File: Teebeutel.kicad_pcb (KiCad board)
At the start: 2 copper layers, 72 x 100 mm, 154 parts, among them J1 RJ45_Shielded, J2 Battery, J3 Micro_SD_Card, J4 Conn_01x30_Female, Q1 S8050, Q2 S8050, SW1 K1-1506SN-01, SW2 SW_SPST, U1 LIS2DE12, U10 SDB628, U11 TLV1117-33, U12 SGP30, U2 ESP32-WROOM-32, U3 SRV05-4, U4 TXB0104RUT, U5 MCP73831-2-OT, U6 PPSI262, U7 RM-V8xxC_TR1, U8 TLV70018_SOT23-5, U9 TXB0104RUT

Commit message: chore(OSHWA): Add ID (DE000117)
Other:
- board text added: "ID: DE000117"
- board text removed: "ID: *TBA*"

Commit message: feat(ibom): add ibom
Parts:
- C1, C10, C11, C12, C13, C14, C15, C16, C17, C19, C2, C20, C22, C24, C25, C27, C3, C32, C35, C38, C5, C6, C7, C9: value 100n -> 100nF
- C18, C21, C23, C26, C29, C31, C37, C4, C40, C8: value 10µ -> 10µF
- C28, C30: value 1µ -> 1µF
- C33, C34: value 4,7µ -> 4,7µF
- D11, D19: value D -> DO-214AC
- L1: value L_Core_Iron -> 4,7µH
- R1, R10, R12, R14, R15, R17, R19, R2, R22, R23, R26, R3, R4, R5, R7, R9: value 10k -> 10kΩ
- R11: value 10 -> 10Ω
- R13: value 2k2 -> 2.2kΩ
- R16, R18, R6, R8: value 470 -> 470Ω
- R20: value 300k -> 300kΩ
- R21: value 100k -> 100KΩ
- R24: value 56 -> 56Ω
- R25: value 82 -> 82Ω
- R27: value 560k -> 560kΩ
- R28: value 620k 1% -> 620kΩ 1%
- R29: value 30k 1% -> 30kΩ 1%

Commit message: feat: more routing work
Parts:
- added C41: 10µF, Capacitor_SMD:C_0603_1608Metric, F.Cu at (117.0, 141.8)
- added C42: 100nF, Capacitor_SMD:C_0603_1608Metric, F.Cu at (115.5, 141.8)
- added C43: 100nF, Capacitor_SMD:C_0603_1608Metric, F.Cu at (257.8, 30.0)
- added C44: 10µF, Capacitor_SMD:C_0603_1608Metric, F.Cu at (260.8, 22.2)
- added D20: 1N4148WT, Diode_SMD:D_SOD-523, F.Cu at (118.5, 141.8)
- added J5: Conn_01x10_Female, Connector_PinSocket_2.54mm:PinSocket_1x10_P2.54mm_Vertical_SMD_Pin1Left, F.Cu at (173.9, 100.0)
- added J6: Conn_01x10_Female, Connector_PinSocket_2.54mm:PinSocket_1x10_P2.54mm_Vertical_SMD_Pin1Right, F.Cu at (118.1, 100.0)
- added M1: Motor_DC, Teebeutel_Special_Parts:LNLON-S3070P, F.Cu at (122.1, 141.8)
- added Q3: BSN20, Package_TO_SOT_SMD:SOT-23, F.Cu at (115.6, 145.0)
- added R30: 10kΩ, Resistor_SMD:R_0603_1608Metric, F.Cu at (113.0, 145.2)
- added R31: 10kΩ, Resistor_SMD:R_0603_1608Metric, F.Cu at (251.9, 26.1)
- added R32: 10kΩ, Resistor_SMD:R_0603_1608Metric, F.Cu at (251.7, 29.2)
- added R33: 10kΩ, Resistor_SMD:R_0603_1608Metric, F.Cu at (155.8, 114.5)
- added R34: 10kΩ, Resistor_SMD:R_0603_1608Metric, F.Cu at (165.2, 114.5)
- added TP33: VIBRATION, TestPoint:TestPoint_Pad_D1.0mm, F.Cu at (113.0, 147.8)
- added TP34: EXP-INT-B, TestPoint:TestPoint_Pad_D1.0mm, F.Cu at (264.3, 35.9)
- added TP35: EXP-~RST, TestPoint:TestPoint_Pad_D1.0mm, F.Cu at (263.0, 38.3)
- added U13: PCA9539BS,118, Teebeutel_Special_Parts:QFN50P400X400X100-25N-D, F.Cu at (160.5, 117.0)
- J2: footprint Connector_PinHeader_2.54mm:PinHeader_1x02_P2.54mm_Vertical -> Connector_Molex:Molex_PicoBlade_53261-0271_1x02-1MP_P1.25mm_Horizontal
- moved TP18 174.5 mm to (275.5, 38.1), turned to 0 degrees
- moved TP15 173.0 mm to (277.5, 36.6)
- moved TP14 161.6 mm to (275.0, 32.1)
- moved TP16 160.1 mm to (279.8, 34.3)
- moved TP17 158.9 mm to (278.7, 28.7)
- moved TP4 131.1 mm to (273.4, 72.9)
- moved TP5 129.0 mm to (273.6, 76.2)
- moved R10 125.4 mm to (268.2, 72.5), turned to 0 degrees
- moved R9 124.9 mm to (268.1, 75.5), turned to 0 degrees
- moved TP3 114.2 mm to (245.5, 123.4), turned to 0 degrees
- moved R4 113.9 mm to (242.9, 115.2), turned to 0 degrees
- moved TP1 113.3 mm to (242.4, 122.9), turned to 0 degrees
- moved Q1 110.4 mm to (238.7, 115.1), turned to 0 degrees
- moved R5 109.0 mm to (243.1, 118.3), turned to 0 degrees
- moved Q2 105.8 mm to (239.3, 120.3), turned to 0 degrees
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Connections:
- D12 pad 1: Net-(D12-Pad1) -> WS2812
- D12 pad 3: (no net) -> Net-(D12-Pad3)
- D13 pad 1: Net-(D10-Pad3) -> Net-(D1-Pad3)
- D13 pad 3: Net-(D1-Pad1) -> Net-(D10-Pad1)
- D2 pad 1: WS2812 -> Net-(D2-Pad1)
- D2 pad 3: Net-(D2-Pad3) -> WS2812-OUT
- D3 pad 1: Net-(D1-Pad3) -> Net-(D3-Pad1)
- D3 pad 3: Net-(D3-Pad3) -> Net-(D1-Pad1)
- D4 pad 1: Net-(D2-Pad3) -> Net-(D4-Pad1)
- D4 pad 3: Net-(D4-Pad3) -> Net-(D2-Pad1)
- D5 pad 1: Net-(D3-Pad3) -> Net-(D5-Pad1)
- D5 pad 3: Net-(D5-Pad3) -> Net-(D3-Pad1)
- D6 pad 1: Net-(D4-Pad3) -> Net-(D6-Pad1)
- D6 pad 3: Net-(D6-Pad3) -> Net-(D4-Pad1)
- D7 pad 1: Net-(D5-Pad3) -> Net-(D7-Pad1)
- D7 pad 3: Net-(D7-Pad3) -> Net-(D5-Pad1)
- D8 pad 1: Net-(D6-Pad3) -> Net-(D10-Pad3)
- D8 pad 3: Net-(D10-Pad1) -> Net-(D6-Pad1)
- D9 pad 1: Net-(D7-Pad3) -> Net-(D12-Pad3)
- D9 pad 3: Net-(D12-Pad1) -> Net-(D7-Pad1)
- J2 pad 1: GND -> Net-(C26-Pad1)
- J2 pad 2: Net-(C26-Pad1) -> GND
- J4 pad 14: +3V3 -> GND
- J4 pad 18: OLED-SDA -> OLED-MOSI
- TB1 pad 1: TOUCH9 -> TOUCH0
- TB2 pad 1: TOUCH4 -> TOUCH3
- TP27 pad 1: OLED-SDA -> (no net)
- U2 pad 10: (no net) -> I2C-SCL
- U2 pad 11: (no net) -> I2C-SDA
- U2 pad 12: TOUCH9 -> IR-TX
- U2 pad 13: OLED-SDA -> OLED-SCK
- U2 pad 14: OLED-SCK -> (no net)
- U2 pad 16: OLED-DC -> OLED-MOSI
- U2 pad 17: BTN_PUSH -> (no net)
- U2 pad 18: SD-SCK -> (no net)
- U2 pad 19: SD-MISO -> (no net)
- U2 pad 20: TOUCH4 -> (no net)
- U2 pad 21: BTN_UP -> (no net)
- U2 pad 22: BTN_DOWN -> (no net)
- U2 pad 23: SD-MOSI -> TOUCH3
- U2 pad 26: SD-CS -> TOUCH0
- U2 pad 29: I2C-SDA -> SD-CS
- U2 pad 30: I2C-SCL -> SD-SCK
- U2 pad 31: WS2812 -> SD-MISO
- U2 pad 33: BTN_LEFT -> OLED-DC
- U2 pad 34: TxD -> RxD
- U2 pad 35: RxD -> TxD
- U2 pad 36: BTN_RIGHT -> EXP-~RST
- U2 pad 37: IR-TX -> SD-MOSI
- U2 pad 6: (no net) -> EXP-~INT
- U2 pad 7: (no net) -> SPO2-INT
- U2 pad 8: (no net) -> WS2812
- U2 pad 9: (no net) -> ESP-ADC5
- U6 pad 9: (no net) -> SPO2-INT
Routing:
- net +3V3: track 568.0 -> 173.2 mm, vias 26 -> 4
- net I2C-SCL: track 106.5 -> 4.33 mm, vias 8 -> 2
- net I2C-SDA: track 99.9 -> 1.61 mm, vias 8 -> 0
- net VIBRATION: track 0.00 -> 73.9 mm, vias 0 -> 2
- net IR-TX: track 143.0 -> 70.7 mm
- net Net-(C26-Pad1): track 73.2 -> 2.94 mm
- net DTR: track 61.1 -> 0.00 mm, vias 2 -> 0
- net RTS: track 59.5 -> 0.00 mm, vias 2 -> 0
- net RxD: track 82.1 -> 24.0 mm, vias 3 -> 1
- net Net-(J1-Pad5): track 56.8 -> 0.00 mm, vias 1 -> 0
- net +5V: track 56.3 -> 0.00 mm, vias 4 -> 0
- net Net-(J1-Pad4): track 55.9 -> 0.00 mm
- net OLED-SDA: track 48.9 -> 0.00 mm, vias 2 -> 0
- net Net-(D14-Pad2): track 48.0 -> 0.00 mm
- net OLED-MOSI: track 0.00 -> 46.7 mm, vias 0 -> 2
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- removed copper zone on F.Cu, net +5V
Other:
- board text added: "3.3V"
- board text added: "BATTERY"
- board text added: "GND"
- board text added: "IO0"
- board text added: "IO1"
- board text added: "IO2"
- board text added: "IO3"
- board text added: "IO4"
- board text added: "IO5"
- board text added: "IO6"
- board text added: "IO7"
- board text added: "IO8"
- board text added: "IO9"
- board text added: "I²C"
- board text added: "LED"
- board text added: "RX"
- board text added: "SCL"
- board text added: "SDA"
- board text added: "SERIAL"
- board text added: "TX"
- board text added: "Teebeutel v1.0"
- board text added: "VIN"
- board text added: "teebeutel.entropia.de"
- board text removed: "Teebeutel v0.1"
- board text removed: "teebeutel.jadyn.dev"

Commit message: small changes
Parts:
- added R35: 10kΩ, Resistor_SMD:R_0603_1608Metric, F.Cu at (195.0, 67.5)
- Q3: value BSN20 -> AO3400
- REF**: value OSHW-Logo2_7.3x6mm_SilkScreen -> OSHW-Logo2_9.8x8mm_SilkScreen; footprint Symbol:OSHW-Logo2_7.3x6mm_SilkScreen -> Symbol:OSHW-Logo2_9.8x8mm_SilkScreen
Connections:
- U6 pad 13: (no net) -> Net-(R35-Pad1)
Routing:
- net SD-MOSI: track 24.2 -> 25.3 mm
- net VIBRATION: track 73.9 -> 74.9 mm
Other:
- outline, holes or cut-outs redrawn

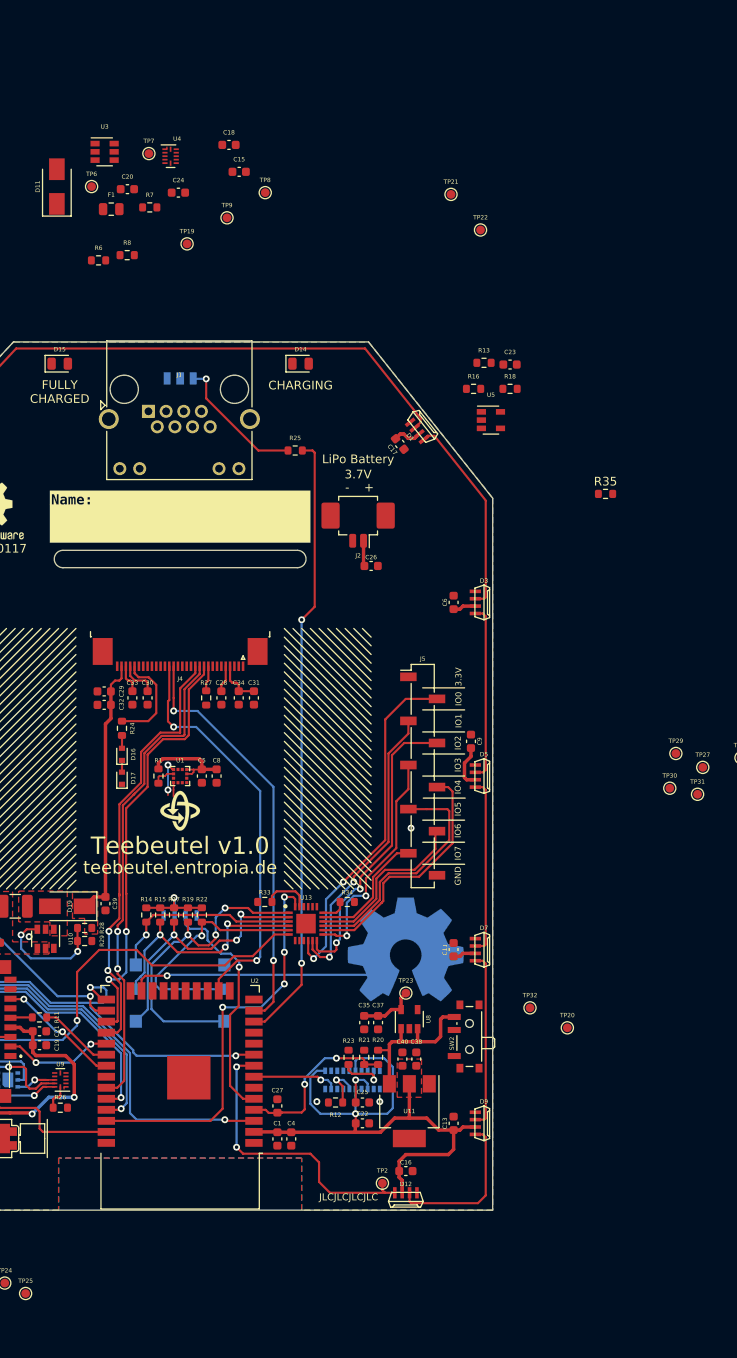
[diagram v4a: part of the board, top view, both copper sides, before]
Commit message: feat(): Change footprints
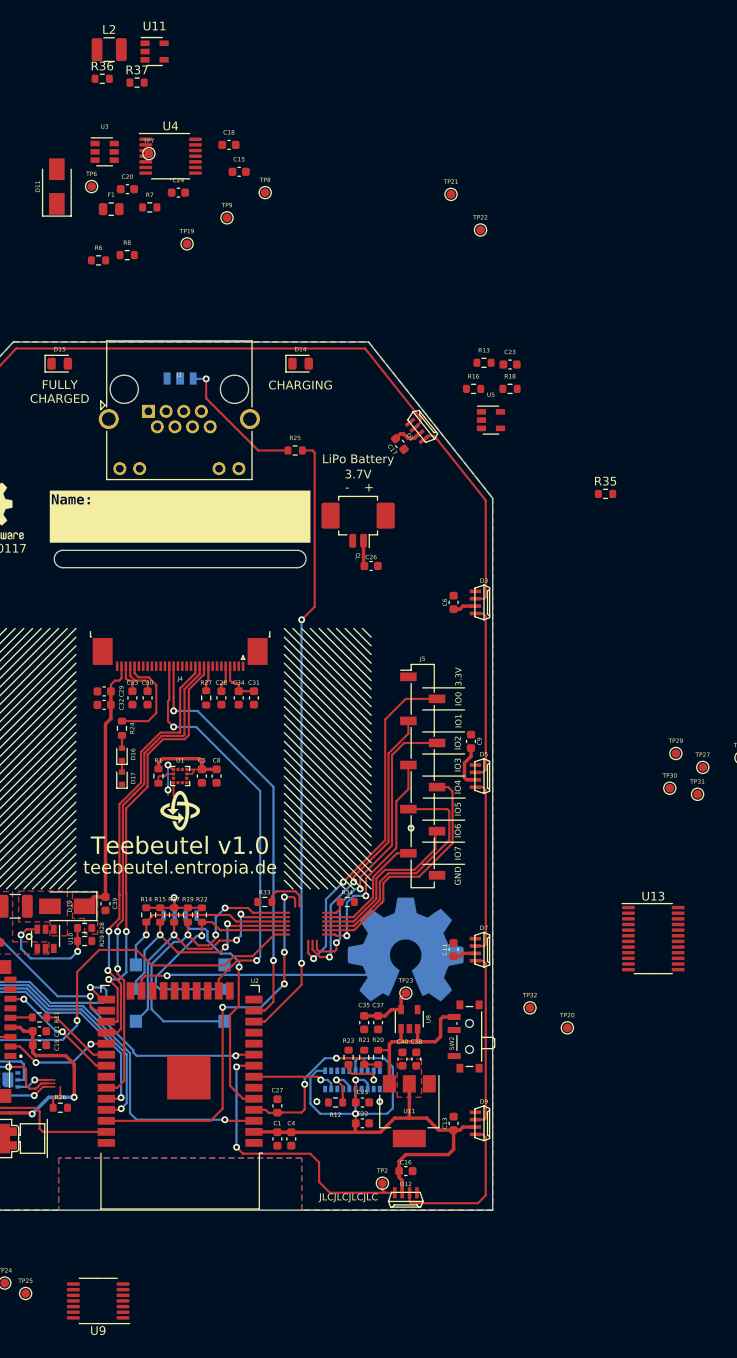
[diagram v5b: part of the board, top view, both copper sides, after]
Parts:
- added L2: 2.2µH, Inductor_SMD:L_1210_3225Metric, F.Cu at (137.8, 16.3)
- added R36: 900kΩ, Resistor_SMD:R_0603_1608Metric, F.Cu at (137.0, 19.7)
- added R37: 200KΩ, Resistor_SMD:R_0603_1608Metric, F.Cu at (141.0, 20.1)
- added U11: TLV62568DBV, Package_TO_SOT_SMD:SOT-23-5, F.Cu at (143.1, 16.5)
- U13: footprint Teebeutel_Special_Parts:QFN50P400X400X100-25N-D -> Package_SO:TSSOP-24_4.4x7.8mm_P0.65mm
- U4, U9: footprint Package_DFN_QFN:Texas_R_PUQFN-N12 -> Package_SO:TSSOP-14_4.4x5mm_P0.65mm
- moved U13 40.0 mm to (200.5, 118.7)
- moved U9 25.8 mm to (136.6, 160.5)
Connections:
- U13 pad 1: BTN_PUSH -> EXP-~INT
- U13 pad 10: EXP-IO1-0 -> (no net)
- U13 pad 11: EXP-IO1-1 -> EXP-IO0-8
- U13 pad 12: EXP-IO1-2 -> GND
- U13 pad 13: EXP-IO1-3 -> EXP-IO1-0
- U13 pad 14: EXP-IO1-4 -> EXP-IO1-1
- U13 pad 15: EXP-IO1-5 -> EXP-IO1-2
- U13 pad 16: EXP-IO1-6 -> EXP-IO1-3
- U13 pad 17: EXP-IO1-7 -> EXP-IO1-4
- U13 pad 18: Net-(R34-Pad1) -> EXP-IO1-5
- U13 pad 19: I2C-SCL -> EXP-IO1-6
- U13 pad 2: BTN_UP -> Net-(R33-Pad1)
- U13 pad 20: I2C-SDA -> EXP-IO1-7
- U13 pad 21: +3V3 -> Net-(R34-Pad1)
- U13 pad 22: EXP-~INT -> I2C-SCL
- U13 pad 23: Net-(R33-Pad1) -> (no net)
- U13 pad 24: EXP-~RST -> +3V3
- U13 pad 3: BTN_DOWN -> EXP-~RST
- U13 pad 4: BTN_LEFT -> BTN_PUSH
- U13 pad 5: BTN_RIGHT -> BTN_UP
- U13 pad 6: VIBRATION -> BTN_DOWN
- U13 pad 7: (no net) -> BTN_LEFT
- U13 pad 8: EXP-IO0-8 -> BTN_RIGHT
- U13 pad 9: GND -> VIBRATION
- U4 pad 10: DTR -> RTS
- U4 pad 11: +3V3 -> RxD
- U4 pad 12: Net-(R7-Pad1) -> TxD
- U4 pad 6: GND -> (no net)
- U4 pad 7: RTS -> GND
- U4 pad 8: RxD -> Net-(R7-Pad1)
- U4 pad 9: TxD -> (no net)
- U9 pad 10: Net-(TP24-Pad1) -> (no net)
- U9 pad 11: +1V8 -> (no net)
- U9 pad 12: Net-(R26-Pad1) -> Net-(TP25-Pad1)
- U9 pad 6: GND -> (no net)
- U9 pad 7: (no net) -> GND
- U9 pad 8: (no net) -> Net-(R26-Pad1)
- U9 pad 9: Net-(TP25-Pad1) -> (no net)

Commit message: chore: cleanup and update to KiCad6
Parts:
- removed R6, R8: 470Ω, Resistor_SMD:R_0603_1608Metric
- removed the U11 at (172.4, 138.6)
- added Q4: AO3400, Package_TO_SOT_SMD:SOT-23, F.Cu at (328.4, -100.0)
- added Q5: AO3400, Package_TO_SOT_SMD:SOT-23, F.Cu at (332.8, -100.0)
- R2, R3: value 10kΩ -> 56Ω
- R36: value 900kΩ -> 900kΩ 1%
- R37: value 200KΩ -> 200kΩ 1%
- TP35: value EXP-~RST -> EXP-~{RST}
- moved R3 239.2 mm to (332.2, -96.4)
- moved R2 234.9 mm to (328.2, -96.4)
- moved U13 40.6 mm to (159.9, 117.4), turned to 90 degrees
- moved U9 25.6 mm to (131.5, 135.4), turned to -90 degrees
- moved R34 13.0 mm to (178.2, 115.2)
- moved R33 11.8 mm to (162.2, 124.3), turned to -90 degrees
- moved R14 11.2 mm to (153.1, 113.8)
- moved R15 8.13 mm to (151.5, 113.8)
- moved R17 5.19 mm to (150.0, 113.8)
- moved R19 2.71 mm to (148.5, 113.8)
- moved R22 2.68 mm to (147.0, 113.8)
- moved R26 1.91 mm to (132.5, 140.1)
- moved C19 1.49 mm to (129.1, 129.7), turned to -90 degrees
- moved R11 1.03 mm to (130.7, 127.3)
- moved C21 0.96 mm to (130.7, 129.7), turned to -90 degrees
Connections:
- net EXP-~INT renamed EXP-~{INT}
- net EXP-~RST renamed EXP-~{RST}
- C20 pad 1: GND -> +5V
- C20 pad 2: +5V -> GND
- C24 pad 1: GND -> +3V3
- C24 pad 2: +3V3 -> GND
- J1 pad 10: Net-(J1-Pad10) -> +3V3
- J1 pad 11: GND -> Net-(J1-Pad11)
- J1 pad 12: Net-(J1-Pad12) -> +3V3
- J1 pad 9: GND -> Net-(J1-Pad9)
- R2 pad 1: GND -> Net-(Q4-Pad3)
- R2 pad 2: RTS -> Net-(J1-Pad11)
- R3 pad 1: GND -> Net-(Q5-Pad3)
- R3 pad 2: DTR -> Net-(J1-Pad9)
- TP25 pad 1: Net-(TP25-Pad1) -> Net-(TP24-Pad1)
- TP7 pad 1: TxD -> RxD
- TP8 pad 1: RxD -> TxD
- U12 pad 3: Net-(TP24-Pad1) -> Net-(U12-Pad3)
- U12 pad 6: Net-(TP25-Pad1) -> Net-(TP24-Pad1)
- U13 pad 23: (no net) -> I2C-SDA
- U13 pad 4: BTN_PUSH -> BTN_DOWN
- U13 pad 5: BTN_UP -> BTN_LEFT
- U13 pad 6: BTN_DOWN -> BTN_UP
- U13 pad 7: BTN_LEFT -> BTN_PUSH
- U4 pad 1: +5V -> +3V3
- U4 pad 10: RTS -> Net-(J1-Pad3)
- U4 pad 11: RxD -> Net-(J1-Pad4)
- U4 pad 12: TxD -> Net-(J1-Pad5)
- U4 pad 13: DTR -> Net-(J1-Pad6)
- U4 pad 14: +3V3 -> +5V
- U4 pad 2: Net-(J1-Pad6) -> DTR
- U4 pad 3: Net-(J1-Pad5) -> RxD
- U4 pad 4: Net-(J1-Pad4) -> TxD
- U4 pad 5: Net-(J1-Pad3) -> RTS
- U9 pad 1: +3V3 -> +1V8
- U9 pad 12: Net-(TP25-Pad1) -> I2C-SCL
- U9 pad 13: Net-(TP24-Pad1) -> I2C-SDA
- U9 pad 14: +1V8 -> +3V3
- U9 pad 2: I2C-SDA -> Net-(U12-Pad3)
- U9 pad 3: I2C-SCL -> Net-(TP24-Pad1)
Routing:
- net VIBRATION: track 74.9 -> 30.9 mm, vias 2 -> 1
- net TOUCH3: track 38.3 -> 9.74 mm, vias 1 -> 0
- net BTN_PUSH: track 36.8 -> 21.1 mm, vias 3 -> 0
- net BTN_RIGHT: track 28.3 -> 15.9 mm, vias 1 -> 0
- net Net-(U12-Pad3): track 0.00 -> 10.8 mm, vias 0 -> 1
- net +3V3: track 173.2 -> 183.9 mm
- net IR-RX: track 27.7 -> 17.4 mm, vias 1 -> 0
- net EXP-IO0-8: track 0.00 -> 9.62 mm
- net EXP-~{RST}: track 46.1 -> 37.5 mm, vias 4 -> 2
- net EXP-IO1-7: track 14.3 -> 22.4 mm
- net EXP-IO1-6: track 19.9 -> 27.0 mm
- net Net-(R33-Pad1): track 5.58 -> 0.00 mm
- net Net-(TP25-Pad1): track 4.58 -> 0.00 mm, vias 1 -> 0
- net EXP-IO1-0: track 40.3 -> 35.9 mm, vias 2 -> 0
- net +1V8: track 24.4 -> 27.6 mm
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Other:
- net class Default removed

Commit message: pcb: finish routing
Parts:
- removed the R32 at (251.7, 29.2)
- removed the TP14 at (275.0, 32.1)
- removed the TP15 at (277.5, 36.6)
- removed the TP16 at (279.8, 34.3)
- removed the TP17 at (278.7, 28.7)
- removed the TP18 at (275.5, 38.1)
- removed the TP19 at (146.8, 38.7)
- removed the TP7 at (142.4, 28.3)
- removed the TP8 at (155.8, 32.8)
- added C38: 4,7µF, Capacitor_SMD:C_0603_1608Metric, F.Cu at (174.8, 131.7)
- added TP10: Charging status, TestPoint:TestPoint_Pad_D1.0mm, F.Cu at (156.8, 56.6)
- TP14: renamed from TP35; value EXP-~{RST} -> EXP-~RST
- moved Q4 279.6 mm to (115.6, 76.1), turned to 180 degrees
- moved Q3 273.6 mm to (115.6, 72.0), turned to 180 degrees
- moved R6 271.6 mm to (115.6, 67.5)
- moved R4 269.5 mm to (115.6, 69.2)
- moved TP14 163.2 mm to (135.1, 139.7)
- moved TP4 141.4 mm to (134.9, 101.5)
- moved TP13 140.9 mm to (161.6, 132.3)
- moved C32 139.5 mm to (155.7, 113.9), turned to 180 degrees
- moved TP5 139.0 mm to (136.9, 101.5)
- moved R13 134.9 mm to (158.2, 123.1), turned to 90 degrees
- moved R5 134.8 mm to (135.1, 98.0), turned to -90 degrees
- moved R7 134.0 mm to (136.7, 98.0), turned to -90 degrees
- moved C30 131.2 mm to (155.7, 112.4), turned to 180 degrees
- moved R31 123.8 mm to (174.2, 137.8)
- moved R32 123.7 mm to (174.2, 139.3), turned to 180 degrees
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- renumbered C15 to C12, C12 to C13, C18 to C14, C13 to C15, C14 to C16, C16 to C17, C17 to C18, C20 to C19, C24 to C20, C42 to C21, C41 to C22, C19 to C23, C23 to C24, C21 to C25, C22 to C26, C25 to C27, C26 to C28, C27 to C29, C43 to C30, C35 to C31, C44 to C32, C37 to C33, C28 to C34, C29 to C35, C30 to C36, C31 to C37, C36 to C39, C32 to C40, C33 to C41, C34 to C42, C38 to C43, C39 to C44, C40 to C45, D13 to D1, D4 to D10, D3 to D11, D20 to D12, D2 to D13, D1 to D14, D14 to D15, D15 to D16, D18 to D17, D16 to D18, D17 to D19, D12 to D2, D19 to D20, D10 to D3, D9 to D4, D8 to D5, D7 to D6, D11 to D7, D6 to D8, D5 to D9, J6 to J2, J5 to J3, J2 to J4, J3 to J5, J4 to J6, Q4 to Q3, Q5 to Q4, Q3 to Q5, R13 to R10, R16 to R11, R11 to R12, R31 to R13, R33 to R14, R12 to R15, R34 to R16, R14 to R17, R15 to R18, R18 to R19, R4 to R2, R17 to R20, R20 to R21, R21 to R22, R19 to R23, R22 to R24, R23 to R25, R35 to R26, R25 to R27, R24 to R28, R26 to R29, R5 to R3, R27 to R30, R36 to R31, R37 to R32, R28 to R33, R29 to R34, R2 to R4, R9 to R5, R3 to R6, R10 to R7, R30 to R8, R7 to R9, SW2 to SW1, SW1 to SW2, TP13 to TP12, TP34 to TP13, TP12 to TP15, TP20 to TP16, TP21 to TP17, TP23 to TP18, TP22 to TP19, TP24 to TP20, TP25 to TP21, TP26 to TP22, TP27 to TP23, TP28 to TP24, TP29 to TP25, TP30 to TP26, TP31 to TP27, TP32 to TP28, TP33 to TP6, TP6 to TP7, TP9 to TP8, TP10 to TP9, U9 to U10, U10 to U12, U12 to U13, U13 to U6, U6 to U7, U7 to U9
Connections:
- C28 pad 1: Net-(C26-Pad1) -> Net-(C28-Pad1)
- J3 pad 2: EXP-IO1-0 -> EXP-IO1-7
- J3 pad 3: EXP-IO1-1 -> EXP-IO1-6
- J3 pad 4: EXP-IO1-2 -> EXP-IO1-5
- J3 pad 5: EXP-IO1-3 -> EXP-IO1-4
- J3 pad 6: EXP-IO1-4 -> EXP-IO1-3
- J3 pad 7: EXP-IO1-5 -> EXP-IO1-2
- J3 pad 8: EXP-IO1-6 -> EXP-IO1-1
- J3 pad 9: EXP-IO1-7 -> EXP-IO1-0
- J4 pad 1: Net-(C26-Pad1) -> Net-(C28-Pad1)
- J5 pad 1: (no net) -> unconnected-(J5-Pad1)
- J5 pad 8: (no net) -> unconnected-(J5-Pad8)
- J6 pad 19: (no net) -> unconnected-(J6-Pad19)
- J6 pad 2: (no net) -> unconnected-(J6-Pad2)
- J6 pad 25: (no net) -> unconnected-(J6-Pad25)
- J6 pad 6: (no net) -> unconnected-(J6-Pad6)
- J6 pad 7: (no net) -> unconnected-(J6-Pad7)
- J6 pad 8: (no net) -> unconnected-(J6-Pad8)
- SW1 pad 1: (no net) -> unconnected-(SW1-Pad1)
- SW1 pad 2: Net-(C26-Pad1) -> +BATT
- SW1 pad 3: +BATT -> Net-(C28-Pad1)
- TP20 pad 1: Net-(TP24-Pad1) -> Net-(TP20-Pad1)
- TP21 pad 1: Net-(TP24-Pad1) -> Net-(TP21-Pad1)
- TP23 pad 1: (no net) -> OLED-MOSI
- TP7 pad 1: DTR -> RTS
- TP8 pad 1: RTS -> DTR
- U1 pad 11: (no net) -> unconnected-(U1-Pad11)
- U1 pad 12: (no net) -> unconnected-(U1-Pad12)
- U1 pad 3: (no net) -> unconnected-(U1-Pad3)
- U10 pad 10: (no net) -> unconnected-(U10-Pad10)
- U10 pad 11: (no net) -> unconnected-(U10-Pad11)
- U10 pad 2: Net-(U12-Pad3) -> Net-(TP20-Pad1)
- U10 pad 3: Net-(TP24-Pad1) -> Net-(TP21-Pad1)
- U10 pad 4: (no net) -> unconnected-(U10-Pad4)
- U10 pad 5: (no net) -> unconnected-(U10-Pad5)
- U10 pad 6: (no net) -> unconnected-(U10-Pad6)
- U10 pad 9: (no net) -> unconnected-(U10-Pad9)
- U12 pad 6: (no net) -> unconnected-(U12-Pad6)
- U13 pad 3: Net-(U12-Pad3) -> Net-(TP20-Pad1)
- U13 pad 4: (no net) -> unconnected-(U13-Pad4)
- U13 pad 6: Net-(TP24-Pad1) -> Net-(TP21-Pad1)
- U2 pad 14: (no net) -> unconnected-(U2-Pad14)
- U2 pad 17: (no net) -> unconnected-(U2-Pad17)
- U2 pad 18: (no net) -> unconnected-(U2-Pad18)
- U2 pad 19: (no net) -> unconnected-(U2-Pad19)
- U2 pad 20: (no net) -> unconnected-(U2-Pad20)
- U2 pad 21: (no net) -> unconnected-(U2-Pad21)
- U2 pad 22: (no net) -> unconnected-(U2-Pad22)
- U2 pad 24: (no net) -> unconnected-(U2-Pad24)
- U2 pad 32: (no net) -> unconnected-(U2-Pad32)
- U4 pad 10: Net-(J1-Pad3) -> Net-(J1-Pad6)
- U4 pad 11: Net-(J1-Pad4) -> Net-(J1-Pad5)
- U4 pad 12: Net-(J1-Pad5) -> Net-(J1-Pad4)
- U4 pad 13: Net-(J1-Pad6) -> Net-(J1-Pad3)
- U4 pad 2: DTR -> RTS
- U4 pad 3: RxD -> TxD
- U4 pad 4: TxD -> RxD
- U4 pad 5: RTS -> DTR
- U4 pad 6: (no net) -> unconnected-(U4-Pad6)
- U4 pad 9: (no net) -> unconnected-(U4-Pad9)
- U5 pad 3: Net-(C26-Pad1) -> Net-(C28-Pad1)
- U6 pad 10: (no net) -> unconnected-(U6-Pad10)
- U6 pad 4: BTN_DOWN -> BTN_RIGHT
- U6 pad 5: BTN_LEFT -> BTN_PUSH
- U6 pad 7: BTN_PUSH -> BTN_LEFT
- U6 pad 8: BTN_RIGHT -> BTN_DOWN
- U7 pad 1: (no net) -> unconnected-(U7-Pad1)
- U7 pad 10: (no net) -> unconnected-(U7-Pad10)
- U7 pad 12: (no net) -> unconnected-(U7-Pad12)
- U7 pad 14: (no net) -> unconnected-(U7-Pad14)
- U7 pad 17: (no net) -> unconnected-(U7-Pad17)
- U7 pad 2: (no net) -> unconnected-(U7-Pad2)
- U7 pad 20: (no net) -> unconnected-(U7-Pad20)
- U7 pad 4: (no net) -> unconnected-(U7-Pad4)
- U8 pad 4: (no net) -> unconnected-(U8-Pad4)
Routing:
- net +3V3: track 183.9 -> 701.3 mm, vias 4 -> 24
- net I2C-SDA: track 1.61 -> 145.2 mm, vias 0 -> 10
- net I2C-SCL: track 4.33 -> 145.6 mm, vias 2 -> 12
- net +5V: track 0.00 -> 116.7 mm, vias 0 -> 4
- net VIBRATION: track 30.9 -> 107.7 mm, vias 1 -> 4
- net Net-(C28-Pad1): track 0.00 -> 68.4 mm
- net RxD: track 24.0 -> 87.7 mm, vias 1 -> 6
- net EXP-IO0-8: track 9.62 -> 71.9 mm, vias 0 -> 2
- net TxD: track 26.3 -> 85.4 mm, vias 1 -> 6
- net Net-(D15-Pad1): track 0.00 -> 53.0 mm, vias 0 -> 2
- net +1V8: track 27.6 -> 80.2 mm, vias 1 -> 3
- net WS2812-OUT: track 0.00 -> 50.1 mm, vias 0 -> 2
- net RTS: track 0.00 -> 50.1 mm, vias 0 -> 2
- net DTR: track 0.00 -> 48.3 mm
- net ESP-ADC5: track 21.4 -> 68.6 mm, vias 1 -> 4
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- added copper zone on F.Cu, net Net-(L2-Pad1)

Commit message: chore: Update version numbers and urls
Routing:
- net EXP-IO1-5: track 31.9 -> 31.3 mm
- net EXP-IO1-2: track 19.0 -> 18.4 mm
- net EXP-IO1-4: track 25.4 -> 24.8 mm
- net EXP-IO1-3: track 25.5 -> 24.9 mm
- net EXP-IO1-1: track 19.1 -> 18.5 mm
- net EXP-IO1-6: track 31.7 -> 31.2 mm
- net EXP-IO1-0: track 12.6 -> 12.0 mm
- net EXP-IO1-7: track 38.2 -> 37.7 mm
- net GND: vias 37 -> 38
